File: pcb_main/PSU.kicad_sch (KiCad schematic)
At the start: 25 parts, among them IC101 OPA277, IC102 OPA277, Q101 BD249C, Q102 BD249C, Q103 BC557, Q104 Q_NPN_BCE, U101 ATmega8A-A, U102 MC78L05, U103 MC79L05

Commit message: transistors aligned
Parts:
- removed Q102: BD249C, Package_TO_SOT_THT:TO-247-3_Horizontal_TabDown, symbol Transistor_BJT:BD249C
- removed Q104: Q_NPN_BCE, Package_TO_SOT_THT:TO-220-3_Horizontal_TabDown, symbol Device:Q_NPN_BCE
- added C103: 10n, Capacitor_SMD:C_0603_1608Metric, symbol Device:C_Small
- added Q102, Q105, Q107: BD139, Package_TO_SOT_THT:TO-126-3_Horizontal_TabUp, symbol Transistor_BJT:BD139
- added Q103, Q106: BD249C, Package_TO_SOT_THT:TO-247-3_Horizontal_TabUp, symbol Transistor_BJT:BD249C
- added R105: 220m, Resistor_THT:R_Axial_DIN0414_L11.9mm_D4.5mm_P15.24mm_Horizontal, symbol Device:R
- IC101, IC102: Availability Not in stock -> (none); Check_prices https://www.snapeda.com/parts/OPA277/Texas+Instruments/view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 -> (none); Package None -> (none); Price None -> (none); SnapEDA_Link https://www.snapeda.com/parts/OPA277/Texas+Instruments/view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 -> (none)
- Q101: footprint Package_TO_SOT_THT:TO-247-3_Horizontal_TabDown -> Package_TO_SOT_THT:TO-247-3_Horizontal_TabUp
- R103: footprint Resistor_SMD:R_0603_1608Metric -> Resistor_SMD:R_2512_6332Metric; MPN (none) -> LRP12FTDRR015; Power rating (none) -> 3W; TCR (none) -> 50ppm/C; Tolerance (none) -> 1%
- renumbered C103 to C104, Q103 to Q104, R105 to R106, R106 to R107, R107 to R109
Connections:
- net VCC: now also Q102.2 (C), Q103.2 (C), Q105.2 (C), Q106.2 (C), Q107.2 (C)
- net VEE: now also C103.1
- net at Q101.1 (B): now also Q102.1 (E)
- net pwr_e2: now reaches R104.1
- net pwr_e2: now also Q103.3 (E)
- net pwr_e: now reaches R101.2, R103.1, R104.2, R106.1
- net pwr_e: now also R105.2
- net pwr_b: now reaches D101.2 (A), D102.2 (A), Q104.1 (C)
- net pwr_b: now also Q102.3 (B), Q105.3 (B), Q107.3 (B)
- net I_set: now reaches IC101.3
- net at D103.2 (A), D104.1 (K), IC102.3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: now also C103.2
- net pwr_e1: now reaches Q101.3 (E), R101.1
- net U_set: now reaches R107.1
- new net: Q103.1 (B), Q105.1 (E)
- new net: Q106.1 (B), Q107.1 (E)
- new net pwr_e3: Q106.3 (E), R105.1
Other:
- moved on the sheet: D103, D104, R103, R106, R107, R108, R109

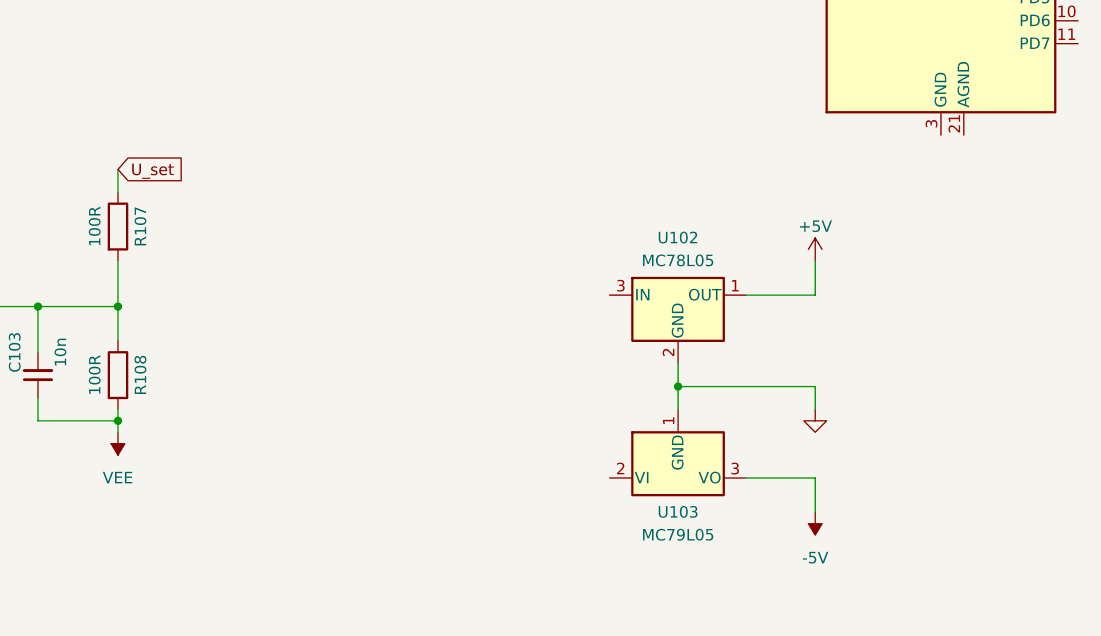
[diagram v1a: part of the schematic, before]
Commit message: +-5V reg
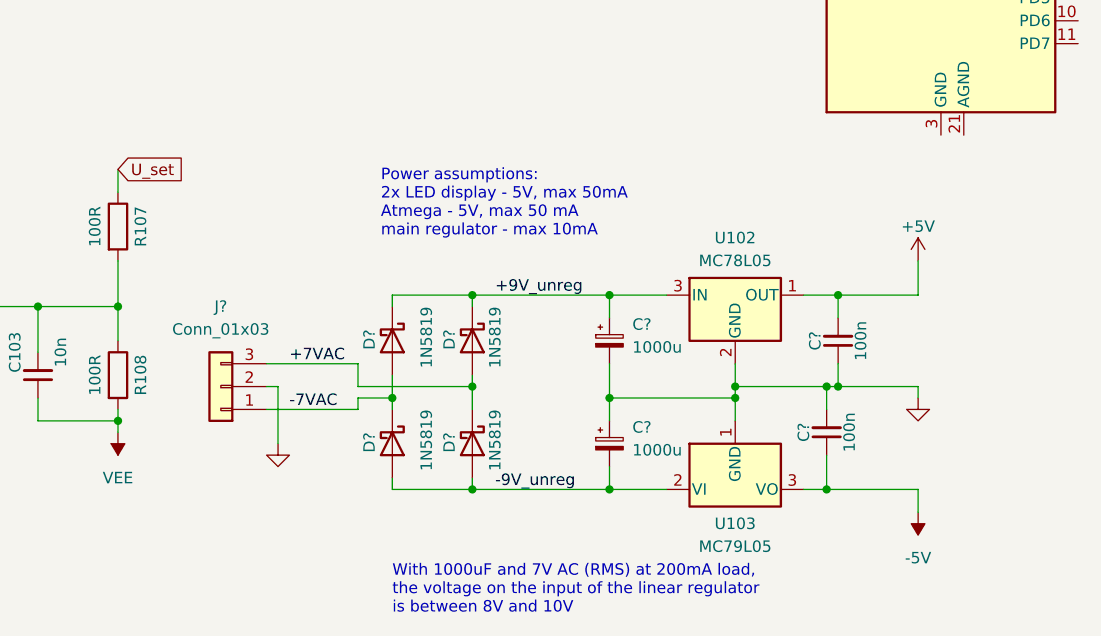
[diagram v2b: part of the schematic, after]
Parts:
- added C? (x2): 1000u, Capacitor_THT:CP_Radial_D8.0mm_P3.50mm, symbol Device:C_Polarized_Small
- added C? (x2): 100n, Capacitor_SMD:C_0603_1608Metric, symbol Device:C_Small
- added D? (x4): 1N5819, Diode_THT:D_DO-41_SOD81_P10.16mm_Horizontal, symbol Diode:1N5819
- added J?: Conn_01x03, Connector_JST:JST_XH_B3B-XH-A_1x03_P2.50mm_Vertical, symbol Connector_Generic:Conn_01x03
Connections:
- net +5V: now also C?.2
- net -5V: now also C?.1
- net GND: now also C?.1, C?.1, C?.2, C?.2, J?.2 (Pin_2)
- net -9V_unreg: now reaches U103.2 (VI)
- net -9V_unreg: now also C?.2, D?.2 (A), D?.2 (A)
- net +9V_unreg: now reaches U102.3 (IN)
- net +9V_unreg: now also C?.1, D?.1 (K), D?.1 (K)
- new net +7VAC: D?.1 (K), D?.2 (A), J?.3 (Pin_3)
- new net -7VAC: D?.1 (K), D?.2 (A), J?.1 (Pin_1)
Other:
- note added: "Power assumptions: 2x LED display - 5V, max 50mA Atmega - 5V, max 50 mA main regulator - max 10mA"
- note added: "With 1000uF and 7V AC (RMS) at 200mA load, the voltage on the input of the linear regulator is between 8V and 10V"
- moved on the sheet: U102, U103

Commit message: hierarchical design
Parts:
- removed C101: 10u, Resistor_SMD:R_0603_1608Metric, symbol Device:C_Small
- removed C102, C104: 22p, Resistor_SMD:R_0603_1608Metric, symbol Device:C_Small
- removed C103: 10n, Capacitor_SMD:C_0603_1608Metric, symbol Device:C_Small
- removed C? (x2): 1000u, Capacitor_THT:CP_Radial_D8.0mm_P3.50mm, symbol Device:C_Polarized_Small
- removed C? (x2): 100n, Capacitor_SMD:C_0603_1608Metric, symbol Device:C_Small
- removed D101, D102, D103, D104: 1N4148WS, Diode_SMD:D_SOD-323, symbol Diode:1N4148WS
- removed D? (x4): 1N5819, Diode_THT:D_DO-41_SOD81_P10.16mm_Horizontal, symbol Diode:1N5819
- removed IC101, IC102: OPA277, OPA277:SO08, symbol OPA277:OPA277
- removed J?: Conn_01x03, Connector_JST:JST_XH_B3B-XH-A_1x03_P2.50mm_Vertical, symbol Connector_Generic:Conn_01x03
- removed Q101, Q103, Q106: BD249C, Package_TO_SOT_THT:TO-247-3_Horizontal_TabUp, symbol Transistor_BJT:BD249C
- removed Q102, Q105, Q107: BD139, Package_TO_SOT_THT:TO-126-3_Horizontal_TabUp, symbol Transistor_BJT:BD139
- removed Q104: BC557, Package_TO_SOT_SMD:SOT-23, symbol Transistor_BJT:BC557
- removed R101, R104, R105: 220m, Resistor_THT:R_Axial_DIN0414_L11.9mm_D4.5mm_P15.24mm_Horizontal, symbol Device:R
- removed R102, R106, R107, R108, R109: 100R, Resistor_SMD:R_0603_1608Metric, symbol Device:R
- removed R103: 15m, Resistor_SMD:R_2512_6332Metric, symbol Device:R
- removed RV101: 4k7, Potentiometer_THT:Potentiometer_Vishay_T73YP_Vertical, symbol Device:R_Potentiometer_Trim
- removed U101: ATmega8A-A, Package_QFP:TQFP-32_7x7mm_P0.8mm, symbol MCU_Microchip_ATmega:ATmega8A-A
- removed U102: MC78L05, Package_TO_SOT_SMD:SOT-89-3, symbol Regulator_Linear:L78L05_SOT89
- removed U103: MC79L05, Package_TO_SOT_SMD:SOT-89-3, symbol Regulator_Linear:L79L05_SOT89
- added J101, J102, J104: JST_XH_B2B-XH, Connector_JST:JST_XH_B2B-XH-A_1x02_P2.50mm_Vertical, symbol Connector_Generic:Conn_01x02
- added J103: JST_XH_B3B-XH, Connector_JST:JST_XH_B3B-XH-A_1x03_P2.50mm_Vertical, symbol Connector_Generic:Conn_01x03
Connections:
- net +7VAC: now also J103.3 (Pin_3)
- net -7VAC: now also J103.1 (Pin_1)
- net GND: now also J101.1 (Pin_1), J103.2 (Pin_2)
- new net main linear regulator/+Vin: J102.2 (Pin_2)
- new net main linear regulator/-Vin: J102.1 (Pin_1)
- new net main linear regulator/-Vout: J101.2 (Pin_2)
- new net power/12VAC1: J104.2 (Pin_2)
- new net power/12VAC2: J104.1 (Pin_1)
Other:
- added sheet MCU (mcu.kicad_sch)
- added sheet main linear regulator (main_regulator.kicad_sch)
- added sheet power (power.kicad_sch)
- note removed: "Power assumptions: 2x LED display - 5V, max 50mA Atmega - 5V, max 50 mA main regulator - max 10mA"
- note removed: "With 1000uF and 7V AC (RMS) at 200mA load, the voltage on the input of the linear regulator is between 8V and 10V"

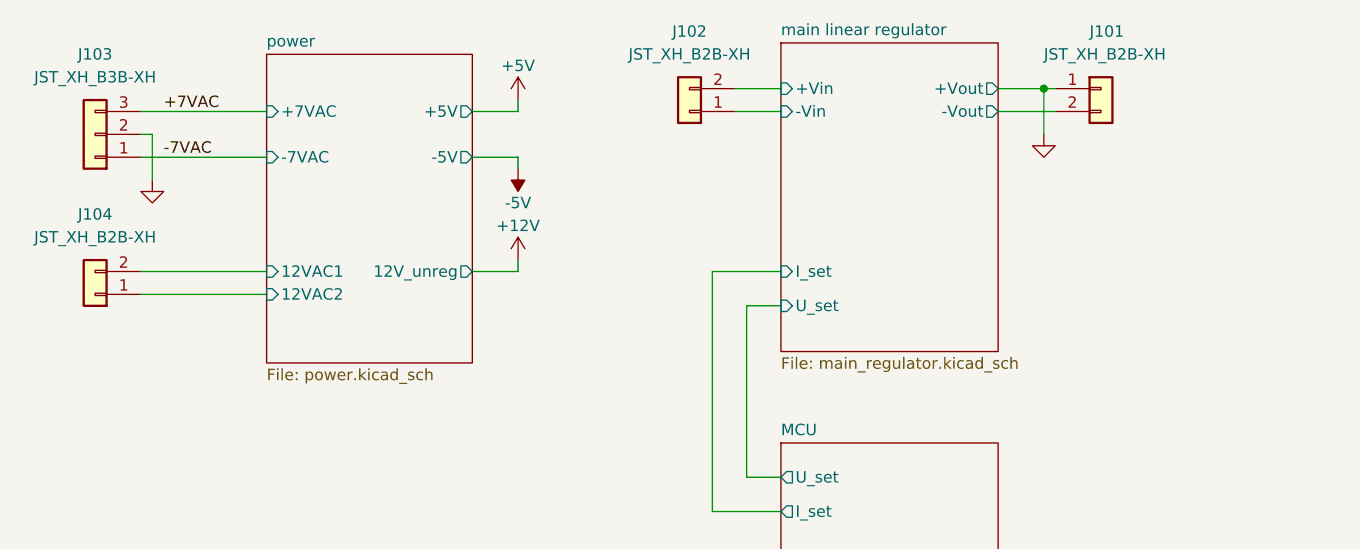
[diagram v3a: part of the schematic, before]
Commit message: power tracks routed
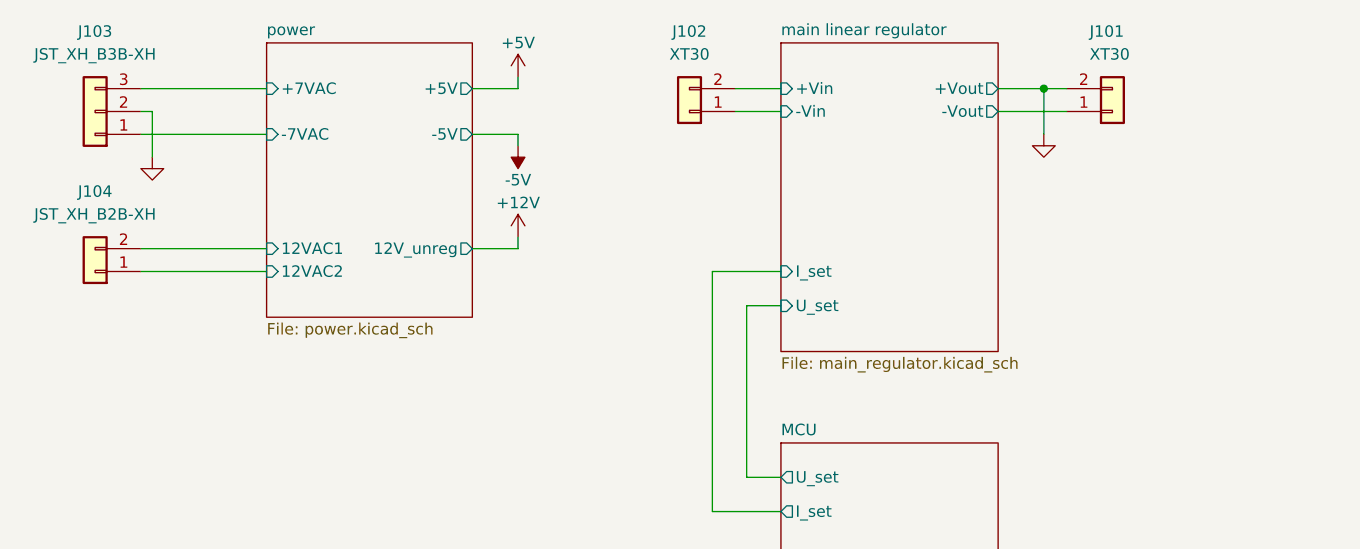
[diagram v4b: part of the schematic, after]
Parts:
- J101, J102: value JST_XH_B2B-XH -> XT30; footprint Connector_JST:JST_XH_B2B-XH-A_1x02_P2.50mm_Vertical -> Connector_AMASS:AMASS_XT30U-M_1x02_P5.0mm_Vertical
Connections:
- net GND: now also J101.2 (Pin_2); no longer J101.1 (Pin_1)
- net main linear regulator/-Vout: now also J101.1 (Pin_1); no longer J101.2 (Pin_2)
- net +7VAC renamed power/+7VAC
- net -7VAC renamed power/-7VAC
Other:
- title: 30V 5A Linear Power Supply -> main sheet
- moved on the sheet: J101, J103, J104
